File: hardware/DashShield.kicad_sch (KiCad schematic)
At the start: 123 parts, among them J001 PWR, J002 Data Logger, J101 CAN0, J102 CAN0, J202 CAN1, J203 CAN0, J3 Dash LEDs, J301 Steering Wheel, J601 GPIO, Q301 2N7002, Q302 2N7002, Q303 2N7002, Q501 2N7002, Q502 2N7002, Q503 2N7002, Q504 2N7002, Q505 2N7002, Q506 2N7002, U101 MCP2515-I/ST, U102 MCP2562-E-SN, U201 MCP2515-I/ST, U202 MCP2562-E-SN, U401 CAT24C256, U601 ADS1015IDGS, Y101 8MHz, Y201 8MHz

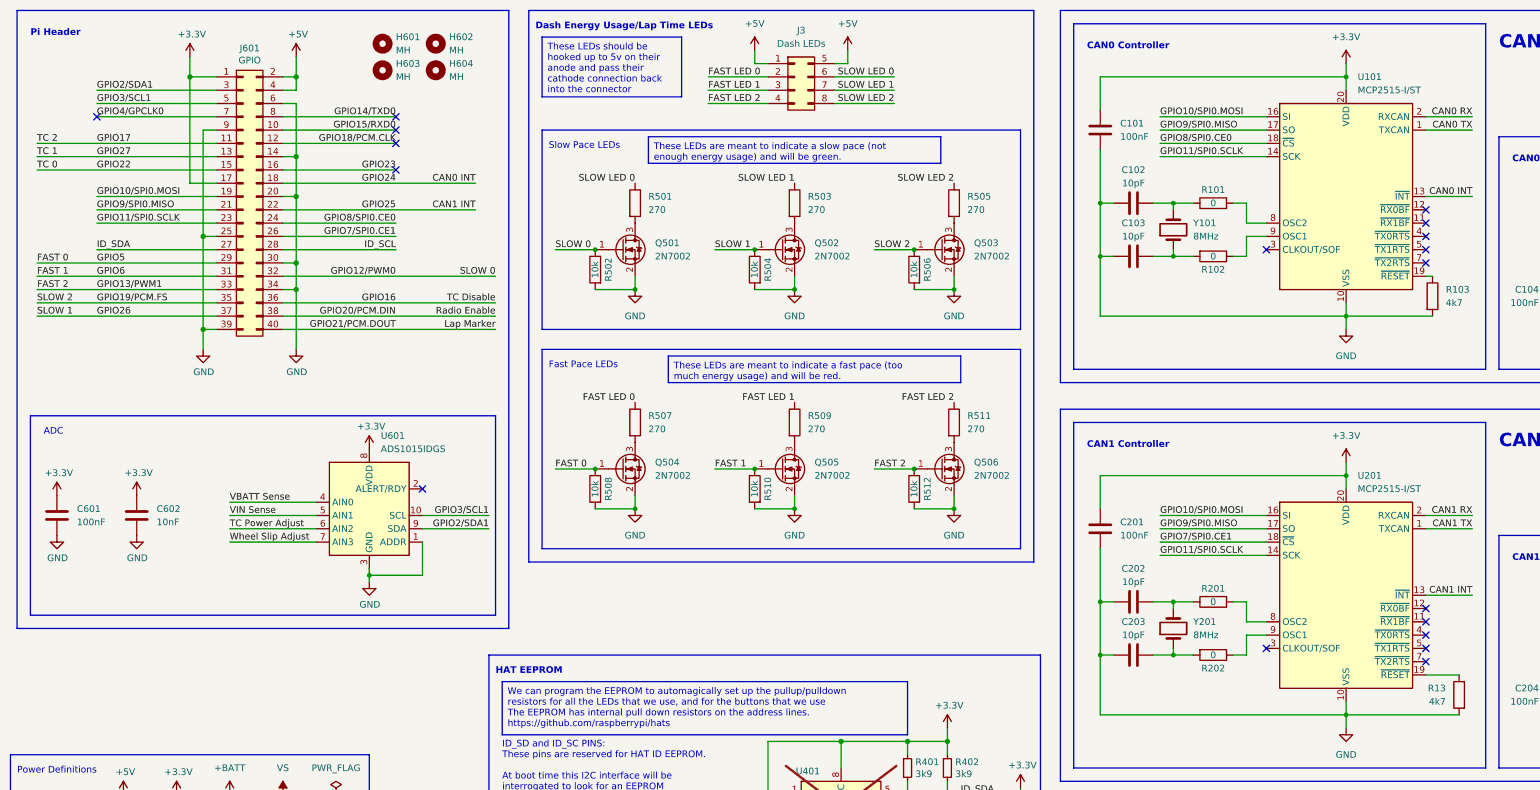
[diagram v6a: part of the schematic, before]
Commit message: chore: I2C pullups and new WIP layout
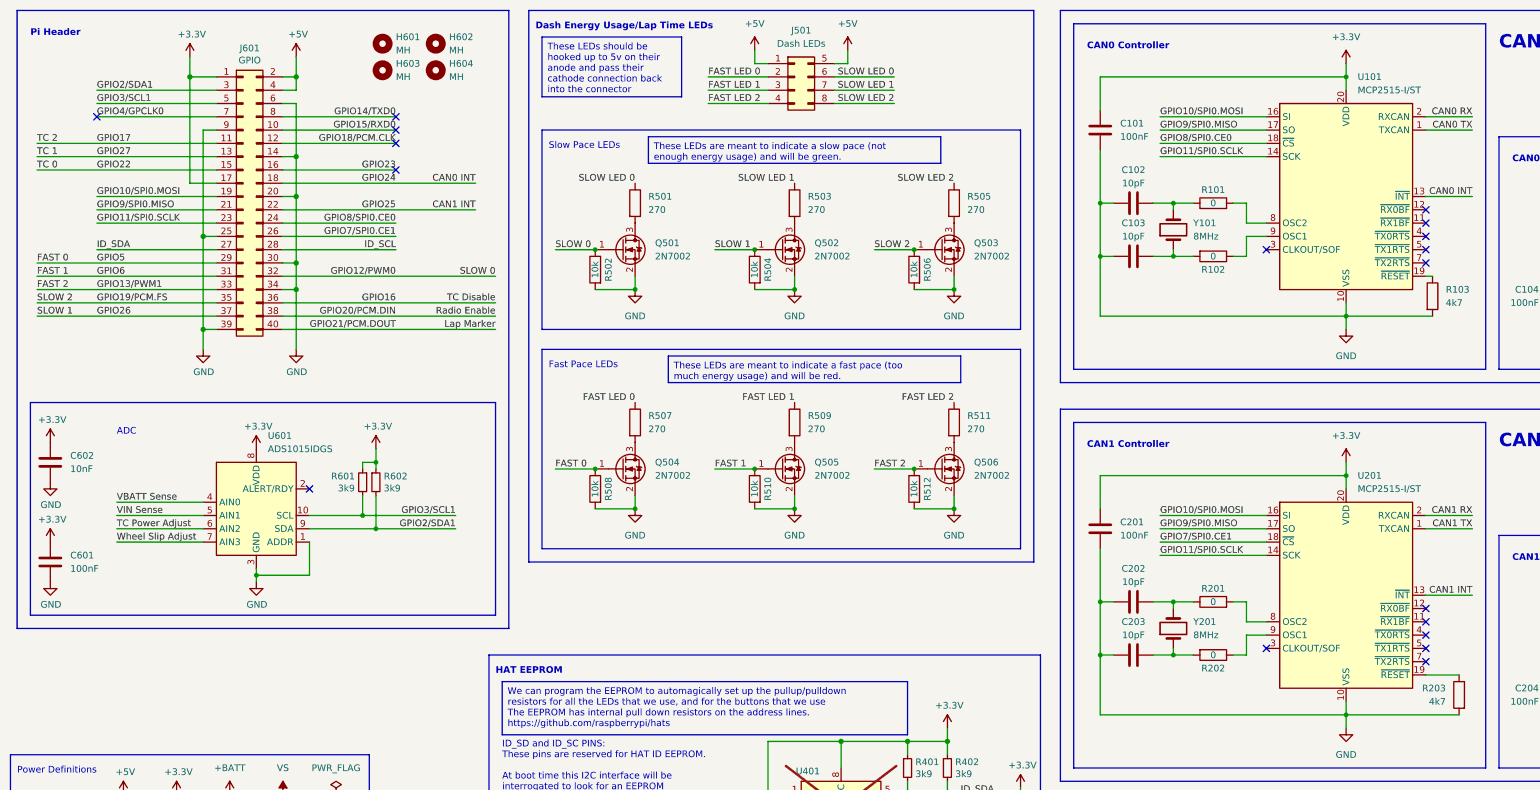
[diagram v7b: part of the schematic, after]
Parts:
- added R601, R602: 3k9, Resistor_SMD:R_0603_1608Metric, symbol Device:R_Small
- renumbered J3 to J501, R13 to R203
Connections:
- net +3.3V: now also R601.1, R602.1
- net GPIO2/SDA1: now also R602.2
- net GPIO3/SCL1: now also R601.2
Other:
- moved on the sheet: C601, C602, U601
